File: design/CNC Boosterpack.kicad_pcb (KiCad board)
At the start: 2 copper layers, 58.4 x 73 mm, 69 parts, among them J1 JP1, J10 EEPROMaddr, J11 UART/GPIO, J2 JP2, J3 JP3, J4 I2CDrv, J5 I2C, J6 RESET, J7 VDrvGND, J8 VDrvSel, J9 Spindle/Coolant, P1 CONN_02x10, P12 YA, P13 YB, P14 ZA, P15 ZB, P17 VMOT, P2 GPIO, P3 Control, P6 XB, P7 CONN_02x10, P8 Limits, P9 XA, Q1 2N7002, Q2 2N7002, Q3 2N7002, Q4 2N7002, U1 TLP290-4, U2 TLP290-4, U3 TLP290-4, U4 24LC16, U5 TCA9406

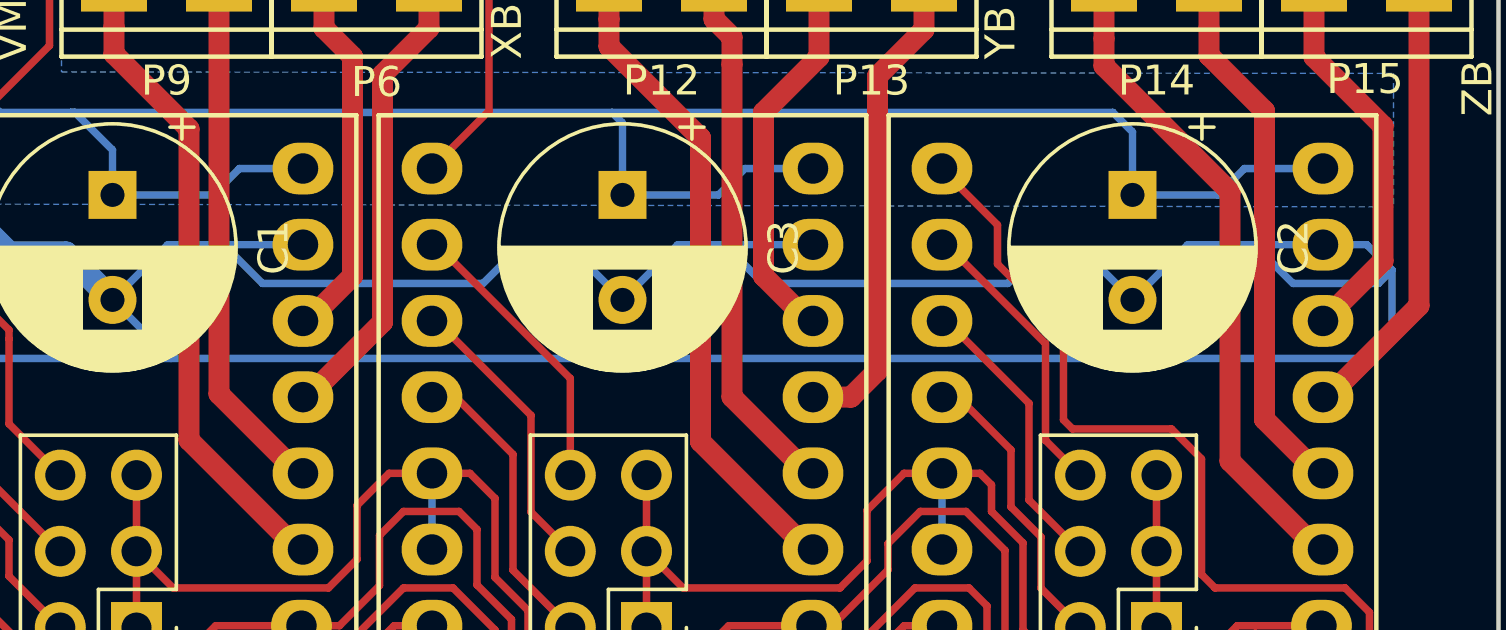
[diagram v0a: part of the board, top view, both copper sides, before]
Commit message: Updated readme and silk screen
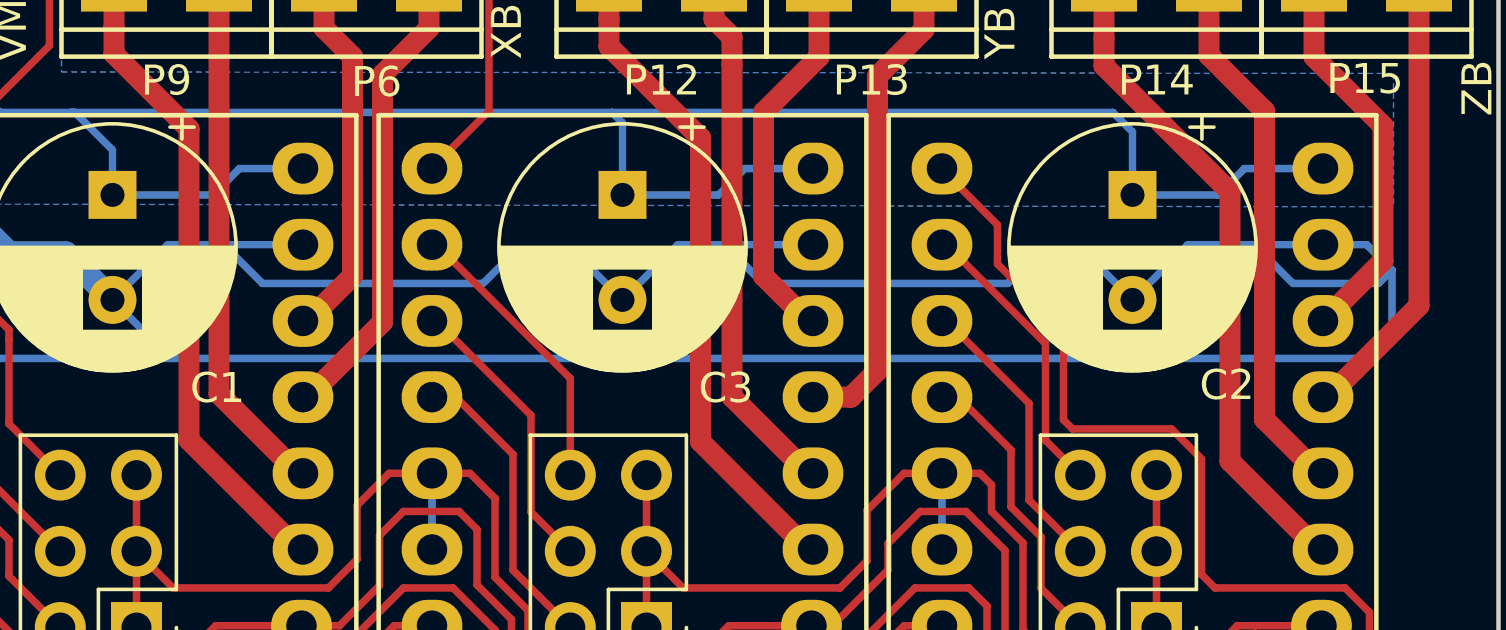
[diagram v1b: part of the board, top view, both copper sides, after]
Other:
- board text added: "GPIO0"
- board text added: "GPIO1"
- board text added: "GPIO2"
- board text added: "GPIO3"
- board text added: "GPIO4/RXD"
- board text added: "GPIO5/TXD"
- board text added: "GPIO6"
- board text added: "I2CDRV"
- board text added: "I2CDrv: west = 3V3, east = 5V"
- board text added: "Motor dummy: A2 = step, A1 = dir, B2 = enable, B1 = VMOT"
- board text added: "SCL"
- board text added: "SDA"
- board text added: "VMOT GND +"
- board text added: "VdrvGnd"
- board text added: "VdrvGnd: open = floating"
- board text added: "VdrvSel: west = external, east = 5V"
- board text added: "X MOTOR A2 A1 B2 B1"
- board text added: "Y MOTOR A2 A1 B2 B1"
- board text added: "Z MOTOR A2 A1 B2 B1"
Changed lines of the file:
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@@
   (general
     (thickness 1.6)
-    (drawings 41)
+    (drawings 65)
     (tracks 1104)
     (zones 0)
@@
     (visible_elements 7FFFFFFF)
     (pcbplotparams
-      (layerselection 0x00004_7ffffffe)
+      (layerselection 0x00120_7ffffffe)
       (usegerberextensions false)
       (usegerberattributes false)
       (usegerberadvancedattributes false)
       (creategerberjobfile false)
-      (excludeedgelayer true)
+      (excludeedgelayer false)
       (linewidth 0.100000)
       (plotframeref false)
       (viasonmask false)
-      (mode 2)
+      (mode 1)
       (useauxorigin false)
       (hpglpennumber 1)
@@
       (psnegative false)
       (psa4output false)
-      (plotreference true)
+      (plotreference false)
       (plotvalue false)
       (plotinvisibletext false)
       (padsonsilk false)
       (subtractmaskfromsilk true)
-      (outputformat 0)
+      (outputformat 4)
       (mirror false)
       (drillshape 0)
@@
     (descr "CP, Radial series, Radial, pin pitch=3.50mm, , diameter=8mm, Electrolytic Capacitor")
     (tags "CP Radial series Radial pin pitch 3.50mm  diameter 8mm Electrolytic Capacitor")
-    (fp_text reference C1 (at 1.75 -5.37 270) (layer F.SilkS)
+    (fp_text reference C1 (at 6.44 -3.5) (layer F.SilkS)
       (effects (font (size 1 1) (thickness 0.15)))
     )
@@
     (descr "CP, Radial series, Radial, pin pitch=3.50mm, , diameter=8mm, Electrolytic Capacitor")
     (tags "CP Radial series Radial pin pitch 3.50mm  diameter 8mm Electrolytic Capacitor")
-    (fp_text reference C2 (at 1.75 -5.37 270) (layer F.SilkS)
+    (fp_text reference C2 (at 6.34 -3.15) (layer F.SilkS)
       (effects (font (size 1 1) (thickness 0.15)))
     )
@@
     (descr "CP, Radial series, Radial, pin pitch=3.50mm, , diameter=8mm, Electrolytic Capacitor")
     (tags "CP Radial series Radial pin pitch 3.50mm  diameter 8mm Electrolytic Capacitor")
-    (fp_text reference C3 (at 1.75 -5.37 270) (layer F.SilkS)
+    (fp_text reference C3 (at 6.44 -3.45) (layer F.SilkS)
       (effects (font (size 1 1) (thickness 0.15)))
     )
@@
     )
   )
+  (gr_text VdrvGnd (at 49.6 3.55 270) (layer Dwgs.User)
+    (effects (font (size 1 1) (thickness 0.15)))
+  )
+  (gr_text "Motor dummy: A2 = step, A1 = dir, B2 = enable, B1 = VMOT" (at 34.4 -78.7) (layer Dwgs.User)
+    (effects (font (size 1 1) (thickness 0.15)))
+  )
+  (gr_text "Z MOTOR\nA2  A1   B2  B1" (at 50.5 -74.9) (layer Dwgs.User)
+    (effects (font (size 1 1) (thickness 0.15)))
+  )
+  (gr_text "Y MOTOR\nA2  A1   B2  B1" (at 34.05 -74.85) (layer Dwgs.User)
+    (effects (font (size 1 1) (thickness 0.15)))
+  )
+  (gr_text "X MOTOR\nA2  A1   B2  B1" (at 17.5 -74.75) (layer Dwgs.User)
+    (effects (font (size 1 1) (thickness 0.15)))
+  )
+  (gr_text "VMOT\nGND +" (at 4.2 -74.8) (layer Dwgs.User)
+    (effects (font (size 1 1) (thickness 0.15)))
+  )
+  (gr_text Reset (at 60.7 -32.5) (layer Dwgs.User)
+    (effects (font (size 1 1) (thickness 0.15)))
+  )
+  (gr_text GND (at 60.35 -29.9) (layer Dwgs.User)
+    (effects (font (size 1 1) (thickness 0.15)))
+  )
+  (gr_text "VdrvSel: west = external, east = 5V" (at 72.55 -8.25) (layer Dwgs.User)
+    (effects (font (size 1 1) (thickness 0.15)))
+  )
+  (gr_text "VdrvGnd: open = floating" (at 68.3 -3.1) (layer Dwgs.User)
+    (effects (font (size 1 1) (thickness 0.15)))
+  )
+  (gr_text GND (at 60.15 -12.1) (layer Dwgs.User)
+    (effects (font (size 1 1) (thickness 0.15)))
+  )
+  (gr_text "I2CDrv: west = 3V3, east = 5V" (at -12.25 -38.95) (layer Dwgs.User)
+    (effects (font (size 1 1) (thickness 0.15)))
+  )
+  (gr_text GPIO5/TXD (at -4.45 -29.85) (layer Dwgs.User)
+    (effects (font (size 1 1) (thickness 0.15)))
+  )
+  (gr_text GPIO4/RXD (at -4.6 -32.35) (layer Dwgs.User)
+    (effects (font (size 1 1) (thickness 0.15)))
+  )
+  (gr_text GND (at -1.9 -27.35) (layer Dwgs.User)
+    (effects (font (size 1 1) (thickness 0.15)))
+  )
+  (gr_text I2CDRV (at -2.9 -22.2) (layer Dwgs.User)
+    (effects (font (size 1 1) (thickness 0.15)))
+  )
+  (gr_text GND (at -1.9 -12.05) (layer Dwgs.User)
+    (effects (font (size 1 1) (thickness 0.15)))
+  )
+  (gr_text "SDA\n" (at -1.95 -14.8) (layer Dwgs.User)
+    (effects (font (size 1 1) (thickness 0.15)))
+  )
+  (gr_text SCL (at -1.95 -17.25) (layer Dwgs.User)
+    (effects (font (size 1 1) (thickness 0.15)))
+  )
+  (gr_text GPIO6 (at -2.7 -19.9) (layer Dwgs.User)
+    (effects (font (size 1 1) (thickness 0.15)))
+  )
+  (gr_text GPIO3 (at 60.85 -14.5) (layer Dwgs.User)
+    (effects (font (size 1 1) (thickness 0.15)))
+  )
+  (gr_text GPIO2 (at 60.8 -17.15) (layer Dwgs.User)
+    (effects (font (size 1 1) (thickness 0.15)))
+  )
+  (gr_text GPIO1 (at 60.8 -19.7) (layer Dwgs.User)
+    (effects (font (size 1 1) (thickness 0.15)))
+  )
+  (gr_text GPIO0 (at 60.9 -22.2) (layer Dwgs.User)
+    (effects (font (size 1 1) (thickness 0.15)))
+  )
   (gr_text Z (at 47.15 -40.85) (layer F.SilkS)
     (effects (font (size 1.5 1.5) (thickness 0.3)))
@@
   (via (at 15.8 -14) (size 0.6) (drill 0.4) (layers F.Cu B.Cu) (net 52))
   (segment (start 15.69 -14.91) (end 15.69 -14.11) (width 0.25) (layer B.Cu) (net 52))
-  (via (at 24.6 -25) (size 0.6) (drill 0.4) (layers F.Cu B.Cu) (net 52))
+  (via (at 24.6 -25) (size 0.6) (drill 0.4) (layers F.Cu B.Cu) (net 52) (status 1000000))
   (segment (start 24.6 -25) (end 24.865 -25.265) (width 0.25) (layer B.Cu) (net 52))
   (segment (start 24.865 -25.265) (end 24.865 -26.7) (width 0.25) (layer B.Cu) (net 52) (status 20))

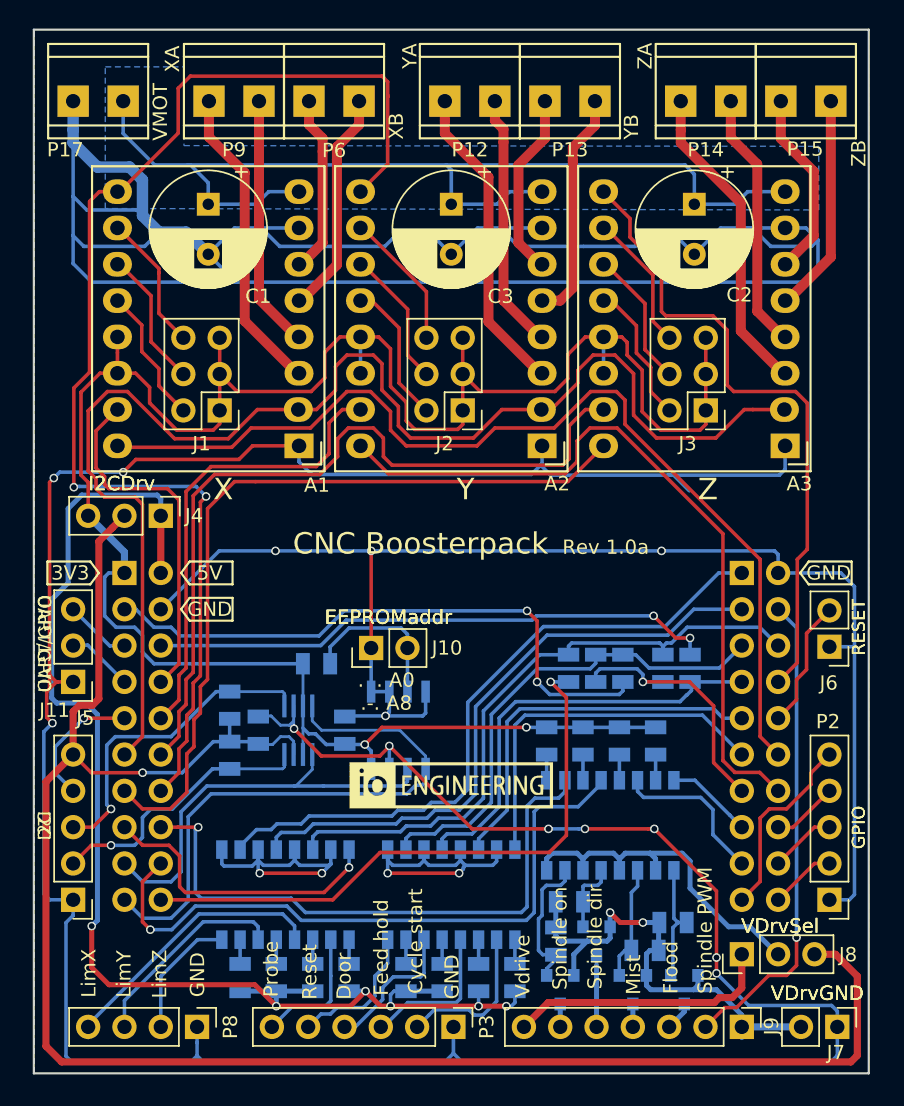
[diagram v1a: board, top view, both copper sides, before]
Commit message: Reduced PCB size
Reduced PCB size to enable two boards to be used with the EK-TM4C1294X
LaunchPad - providing up to 6 axes of control. Update to driver for this
LauncPad underway to  facilitate IP-streaming of jobs.
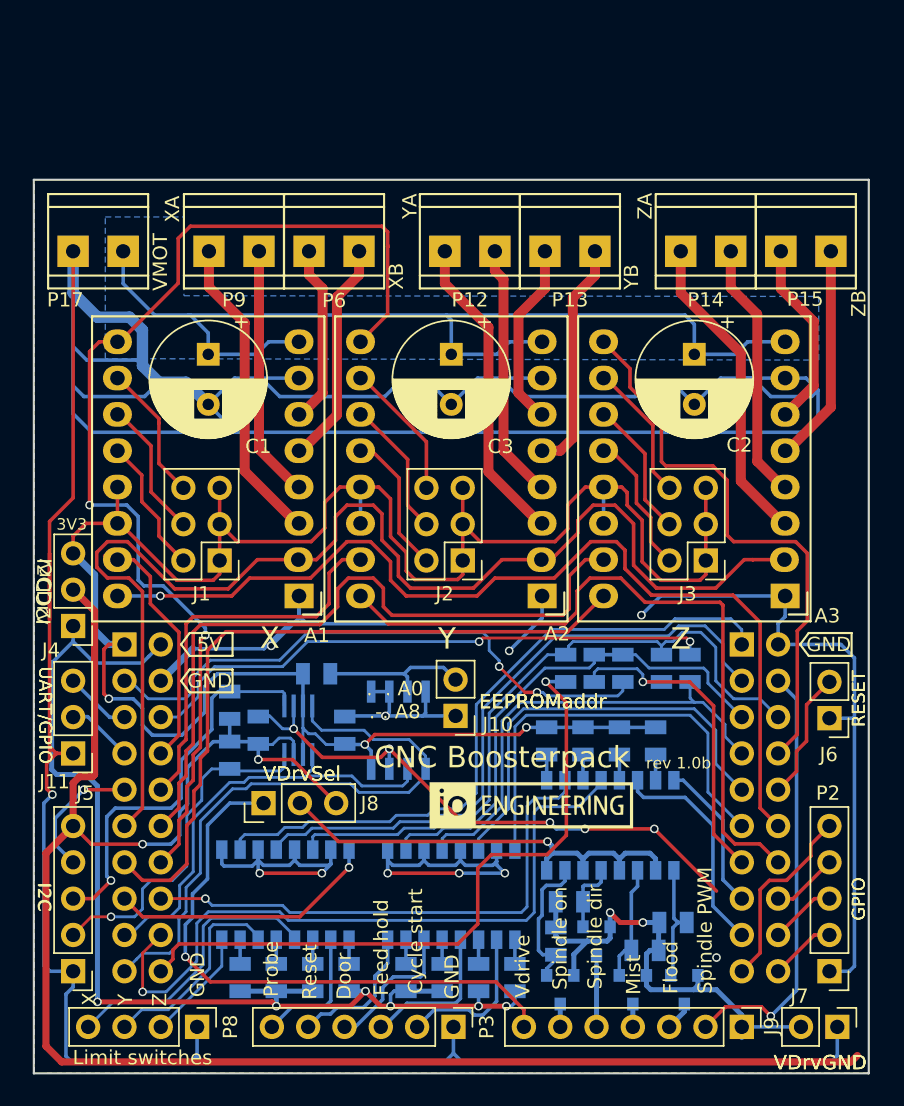
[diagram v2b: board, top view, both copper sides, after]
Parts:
- removed the REF** at (2.55, -35.0)
- moved J8 35.1 mm to (16.1, -18.9)
- moved A1 10.5 mm to (18.6, -33.4)
- moved A2 10.5 mm to (35.5, -33.4)
- moved A3 10.5 mm to (52.5, -33.4)
- moved C1 10.5 mm to (12.2, -50.3)
- moved C2 10.5 mm to (46.2, -50.3)
- moved C3 10.5 mm to (29.2, -50.3)
- moved J1 10.5 mm to (13.0, -35.9)
- moved J2 10.5 mm to (30.0, -35.9)
- moved J3 10.5 mm to (47.0, -35.9)
- moved P12 10.5 mm to (30.5, -57.5)
- moved P13 10.5 mm to (37.5, -57.5)
- moved P14 10.5 mm to (47.0, -57.5)
- moved P15 10.5 mm to (54.0, -57.5)
- moved P17 10.5 mm to (4.50, -57.5)
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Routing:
- net GND: track 513.2 -> 462.7 mm, vias 18 -> 16
- net Net-(J8-Pad1): track 18.7 -> 40.8 mm, vias 0 -> 1
- net /VBUS: track 92.7 -> 80.6 mm
- net /PE1: track 87.0 -> 77.8 mm
- net /PD1: track 25.0 -> 16.9 mm
- net Net-(J8-Pad2): track 24.8 -> 31.2 mm, vias 0 -> 1
- net /PE5: track 93.6 -> 87.2 mm
- net /PF0: track 45.5 -> 40.0 mm
- net /PF1: track 42.7 -> 47.9 mm
- net Net-(J5-Pad2): track 19.3 -> 24.4 mm
- net /PB4: track 55.3 -> 50.2 mm
- net /PE2: track 42.2 -> 37.1 mm
- net /PC7: track 18.6 -> 23.6 mm
- net /PD3: track 55.2 -> 50.3 mm
- net Net-(J5-Pad3): track 22.7 -> 27.6 mm
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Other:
- board size 58.4 x 73 mm -> 58.4 x 62.5 mm
- board text added: "3V3"
- board text added: "I2CDrv: north = 3V3, south = 5V"
- board text added: "Limit switches"
- board text added: "rev 1.0b"
- board text removed: "I2CDrv: west = 3V3, east = 5V"
- board text removed: "LimX"
- board text removed: "LimY"
- board text removed: "LimZ"
- board text removed: "Rev 1.0a"
- board text removed: "VdrvGnd"
